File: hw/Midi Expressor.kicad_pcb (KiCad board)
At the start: 4 copper layers, 76.2 x 59.4 mm, 103 parts, among them J1 USB_C_Receptacle_USB2.0_16P, J11 Exp Connector, J13 Exp Connector, J2 Midi In, J3 Midi Out, J4 Midi Thru, J5 Debug, J7 Exp Connector, J9 Exp Connector, SW1 Reset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

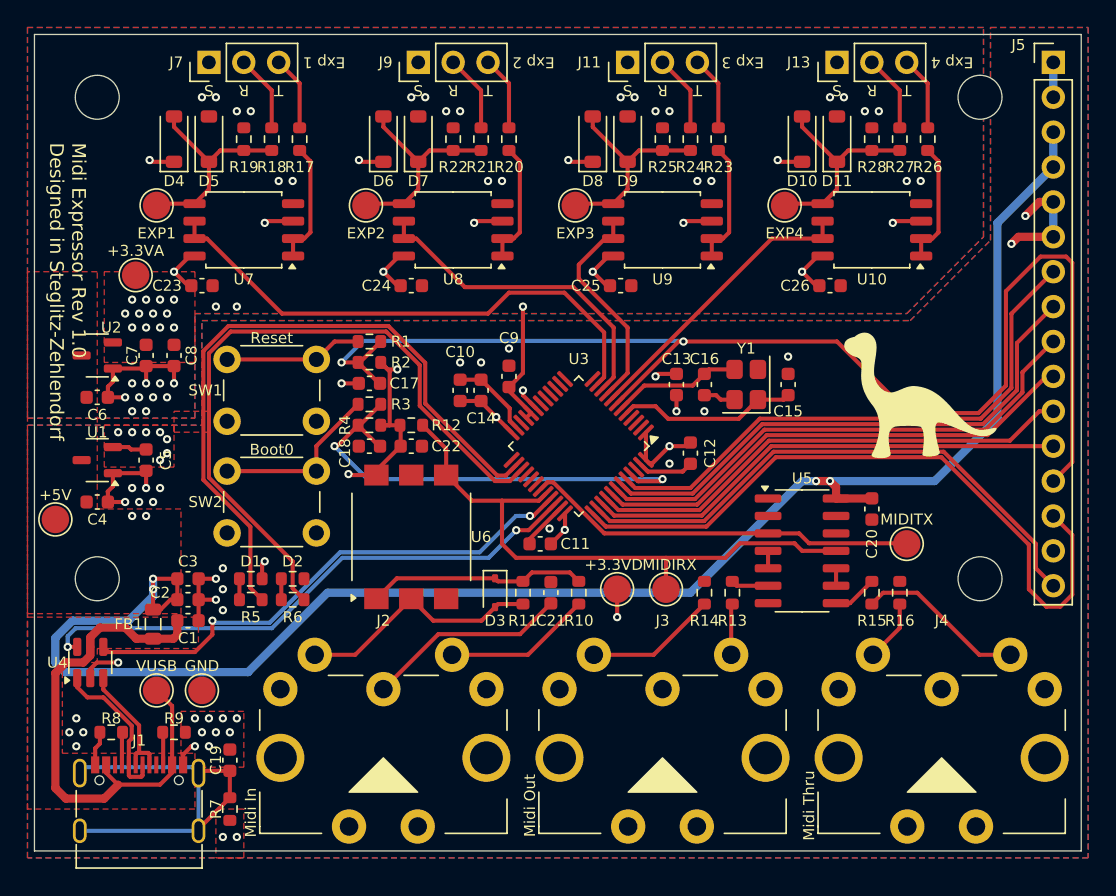
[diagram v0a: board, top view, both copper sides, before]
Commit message: updated hardware issues for PBC revision 2
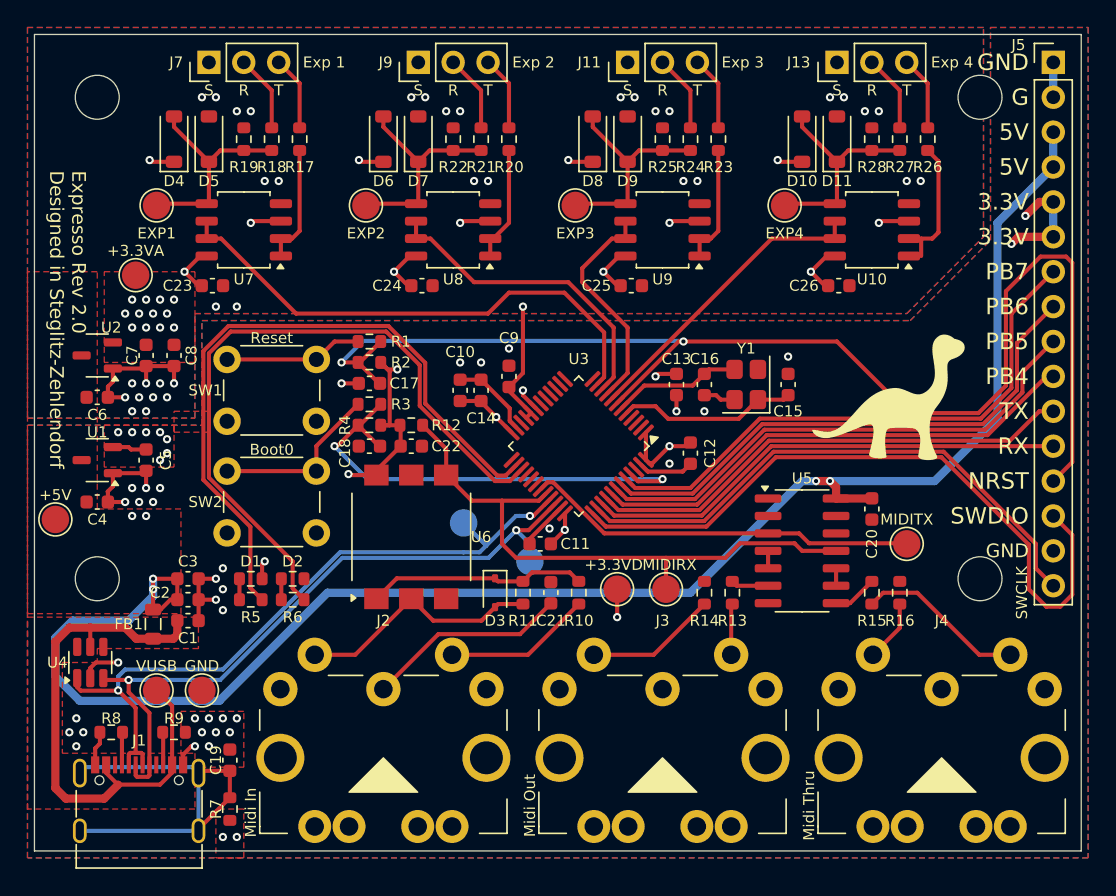
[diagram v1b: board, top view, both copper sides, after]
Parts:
- added TP12: USB D-, TestPoint:TestPoint_Pad_D2.0mm, B.Cu at (154.7, 121.4)
- added TP13: USB D+, TestPoint:TestPoint_Pad_D2.0mm, B.Cu at (159.5, 124.2)
- J2, J3, J4: footprint DIN5_MIDI:DIN5_MIDI -> DIN5_MIDI_MultiGround:DIN5_MIDI_MultiGround
- U10, U7, U8, U9: footprint Package_SO:SOIC-8_5.3x5.3mm_P1.27mm -> NE5532DR:NE5532DR
- moved C24 0.78 mm to (151.7, 104.1)
- moved C25 0.77 mm to (166.9, 104.1)
- moved C23 0.76 mm to (136.4, 104.1)
- moved C26 0.64 mm to (182.0, 104.1)
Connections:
- J1 pad A6: Net-(U4-IO2) -> STM_USB_DP
- J1 pad A7: Net-(U4-IO1) -> STM_USB_DM
- J1 pad B6: Net-(U4-IO2) -> STM_USB_DP
- J1 pad B7: Net-(U4-IO1) -> STM_USB_DM
- U4 pad 1: Net-(U4-IO1) -> STM_USB_DM
- U4 pad 3: Net-(U4-IO2) -> STM_USB_DP
- U4 pad 4: STM_USB_DM -> unconnected-(U4-IO3-Pad4)
- U4 pad 6: STM_USB_DP -> unconnected-(U4-IO4-Pad6)
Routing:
- net STM_USB_DM: track 38.0 -> 51.6 mm
- net Net-(U4-IO1): track 11.4 -> 0.00 mm
- net STM_USB_DP: track 41.0 -> 50.4 mm
- net Net-(U4-IO2): track 9.15 -> 0.00 mm
- net +5V: track 123.1 -> 125.5 mm
- net VUSB: track 38.7 -> 40.7 mm
- net +3.3VA: track 39.7 -> 40.8 mm
- net STM_ADC1_IN3: track 24.0 -> 23.1 mm
- net STM_ADC1_IN4: track 39.1 -> 38.2 mm
- net STM_ADC1_IN1: track 21.4 -> 22.3 mm
- net /Expression Inputs/Expression Input 2/EXP_REF: track 9.01 -> 8.38 mm
- net /Expression Inputs/Expression Input 4/EXP_SENSE: track 15.6 -> 16.1 mm
- net /Expression Inputs/Expression Input 1/EXP_SENSE: track 15.6 -> 16.1 mm
- net /Expression Inputs/Expression Input 3/EXP_SENSE: track 15.6 -> 16.1 mm
- net /Expression Inputs/Expression Input 2/EXP_SENSE: track 15.6 -> 16.1 mm
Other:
- board text added: "3.3V"
- board text added: "5V"
- board text added: "Expresso Rev 2.0 Designed in Steglitz-Zehlendorf"
- board text added: "G"
- board text added: "NRST"
- board text added: "PB4"
- board text added: "PB5"
- board text added: "PB6"
- board text added: "PB7"
- board text added: "RX"
- board text added: "SWCLK"
- board text added: "SWDIO"
- board text added: "TX"
- board text added: "USB D+"
- board text added: "USB D-"
- board text removed: "Midi Expressor Rev 1.0 Designed in Steglitz-Zehlendorf"
